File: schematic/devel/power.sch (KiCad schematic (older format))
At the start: 26 parts

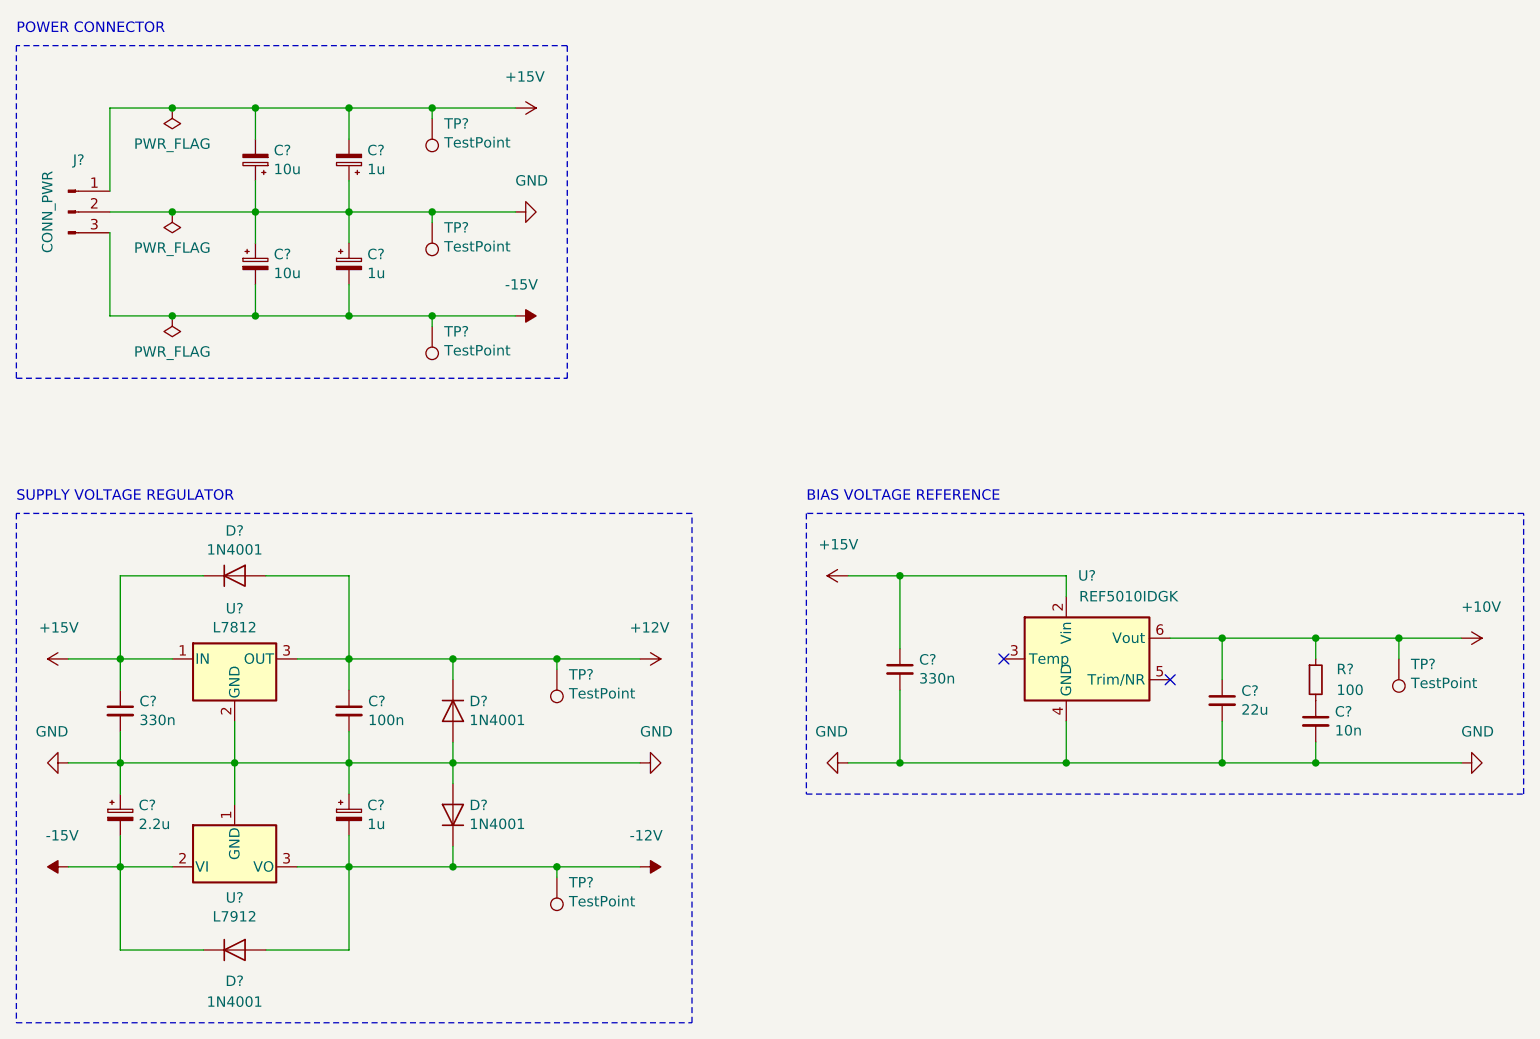
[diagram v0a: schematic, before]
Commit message: fixed floating buffer in arthimetic unit
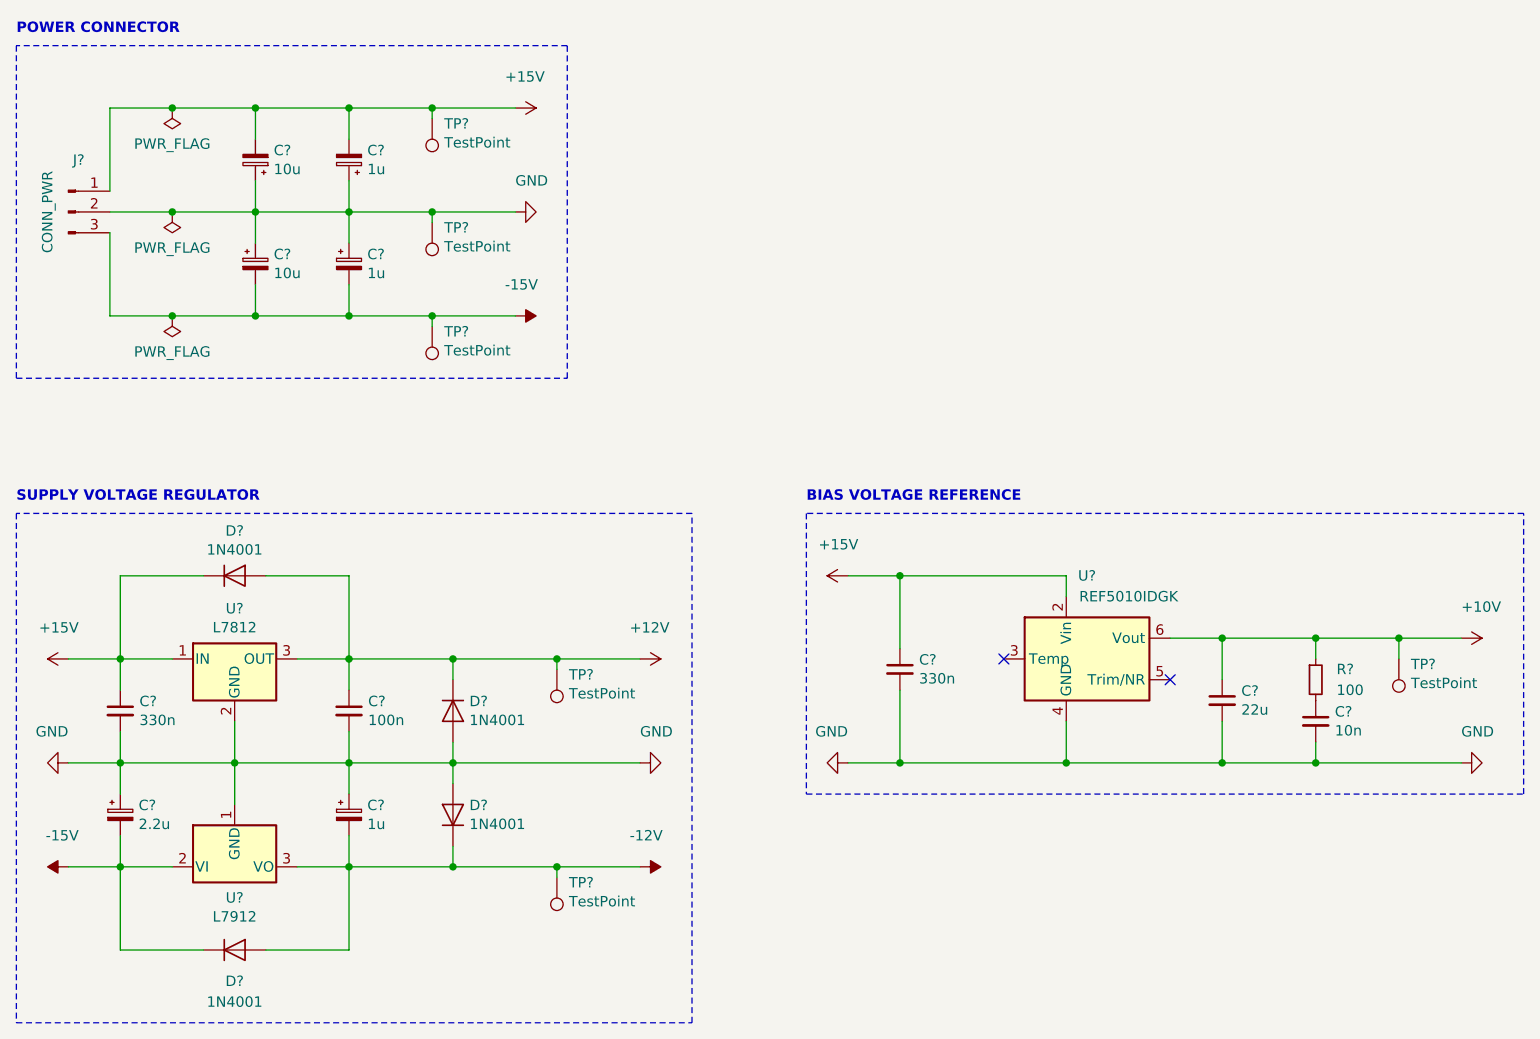
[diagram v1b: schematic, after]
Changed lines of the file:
@@
 Comment4 "Power Management"
 $EndDescr
-Text Notes 700  750  0    50   ~ 0
+Text Notes 700  750  0    50   ~ 6
 POWER CONNECTOR
 Wire Notes Line
@@
 P 3100 1600
 AR Path="/5D81CCB3" Ref="#PWR?"  Part="1"
-AR Path="/5D7CE105/5D81CCB3" Ref="#PWR?"  Part="1"
-F 0 "#PWR?" H 3100 1350 50  0001 C CNN
+AR Path="/5D7CE105/5D81CCB3" Ref="#PWR0101"  Part="1"
+F 0 "#PWR0101" H 3100 1350 50  0001 C CNN
 F 1 "GND" V 3250 1600 50  0000 R CNN
 F 2 "" H 3100 1600 50  0001 C CNN
@@
 P 3100 2100
 AR Path="/5D81CCD6" Ref="#PWR?"  Part="1"
-AR Path="/5D7CE105/5D81CCD6" Ref="#PWR?"  Part="1"
-F 0 "#PWR?" H 3100 2200 50  0001 C CNN
+AR Path="/5D7CE105/5D81CCD6" Ref="#PWR0102"  Part="1"
+F 0 "#PWR0102" H 3100 2200 50  0001 C CNN
 F 1 "-15V" V 2950 2050 50  0000 L CNN
 F 2 "" H 3100 2100 50  0001 C CNN
@@
 P 3100 1100
 AR Path="/5D81CCE3" Ref="#PWR?"  Part="1"
-AR Path="/5D7CE105/5D81CCE3" Ref="#PWR?"  Part="1"
-F 0 "#PWR?" H 3100 950 50  0001 C CNN
+AR Path="/5D7CE105/5D81CCE3" Ref="#PWR0103"  Part="1"
+F 0 "#PWR0103" H 3100 950 50  0001 C CNN
 F 1 "+15V" V 2950 1050 50  0000 L CNN
 F 2 "" H 3100 1100 50  0001 C CNN
@@
 P 1450 1100
 AR Path="/5D81CD0E" Ref="#FLG?"  Part="1"
-AR Path="/5D7CE105/5D81CD0E" Ref="#FLG?"  Part="1"
-F 0 "#FLG?" H 1450 1175 50  0001 C CNN
+AR Path="/5D7CE105/5D81CD0E" Ref="#FLG0101"  Part="1"
+F 0 "#FLG0101" H 1450 1175 50  0001 C CNN
 F 1 "PWR_FLAG" H 1450 1273 50  0000 C CNN
 F 2 "" H 1450 1100 50  0001 C CNN
@@
 P 1450 2100
 AR Path="/5D81CD17" Ref="#FLG?"  Part="1"
-AR Path="/5D7CE105/5D81CD17" Ref="#FLG?"  Part="1"
-F 0 "#FLG?" H 1450 2175 50  0001 C CNN
+AR Path="/5D7CE105/5D81CD17" Ref="#FLG0102"  Part="1"
+F 0 "#FLG0102" H 1450 2175 50  0001 C CNN
 F 1 "PWR_FLAG" H 1450 2273 50  0000 C CNN
 F 2 "" H 1450 2100 50  0001 C CNN
@@
 P 1450 1600
 AR Path="/5D81CD22" Ref="#FLG?"  Part="1"
-AR Path="/5D7CE105/5D81CD22" Ref="#FLG?"  Part="1"
-F 0 "#FLG?" H 1450 1675 50  0001 C CNN
+AR Path="/5D7CE105/5D81CD22" Ref="#FLG0103"  Part="1"
+F 0 "#FLG0103" H 1450 1675 50  0001 C CNN
 F 1 "PWR_FLAG" H 1450 1773 50  0000 C CNN
 F 2 "" H 1450 1600 50  0001 C CNN
@@
 	1    0    0    -1
 $EndComp
-Text Notes 4500 3000 0    50   ~ 0
+Text Notes 4500 3000 0    50   ~ 6
 BIAS VOLTAGE REFERENCE
 Wire Wire Line
@@
 P 7650 3650
 AR Path="/5D891805" Ref="#PWR?"  Part="1"
-AR Path="/5D7CE105/5D891805" Ref="#PWR?"  Part="1"
-F 0 "#PWR?" H 7650 3500 50  0001 C CNN
+AR Path="/5D7CE105/5D891805" Ref="#PWR0104"  Part="1"
+F 0 "#PWR0104" H 7650 3500 50  0001 C CNN
 F 1 "+10V" V 7500 3650 50  0000 L CNN
 F 2 "" H 7650 3650 50  0001 C CNN
@@
 P 7650 4250
 AR Path="/5D89180D" Ref="#PWR?"  Part="1"
-AR Path="/5D7CE105/5D89180D" Ref="#PWR?"  Part="1"
-F 0 "#PWR?" H 7650 4000 50  0001 C CNN
+AR Path="/5D7CE105/5D89180D" Ref="#PWR0105"  Part="1"
+F 0 "#PWR0105" H 7650 4000 50  0001 C CNN
 F 1 "GND" V 7500 4250 50  0000 R CNN
 F 2 "" H 7650 4250 50  0001 C CNN
@@
 P 950 4250
 AR Path="/5D891881" Ref="#PWR?"  Part="1"
-AR Path="/5D7CE105/5D891881" Ref="#PWR?"  Part="1"
-F 0 "#PWR?" H 950 4000 50  0001 C CNN
+AR Path="/5D7CE105/5D891881" Ref="#PWR0106"  Part="1"
+F 0 "#PWR0106" H 950 4000 50  0001 C CNN
 F 1 "GND" V 1100 4250 50  0000 R CNN
 F 2 "" H 950 4250 50  0001 C CNN
@@
 P 950 4750
 AR Path="/5D891887" Ref="#PWR?"  Part="1"
-AR Path="/5D7CE105/5D891887" Ref="#PWR?"  Part="1"
-F 0 "#PWR?" H 950 4850 50  0001 C CNN
+AR Path="/5D7CE105/5D891887" Ref="#PWR0107"  Part="1"
+F 0 "#PWR0107" H 950 4850 50  0001 C CNN
 F 1 "-15V" V 800 4700 50  0000 L CNN
 F 2 "" H 950 4750 50  0001 C CNN
@@
 P 950 3750
 AR Path="/5D89188D" Ref="#PWR?"  Part="1"
-AR Path="/5D7CE105/5D89188D" Ref="#PWR?"  Part="1"
-F 0 "#PWR?" H 950 3600 50  0001 C CNN
+AR Path="/5D7CE105/5D89188D" Ref="#PWR0108"  Part="1"
+F 0 "#PWR0108" H 950 3600 50  0001 C CNN
 F 1 "+15V" V 800 3700 50  0000 L CNN
 F 2 "" H 950 3750 50  0001 C CNN
@@
 P 4700 3350
 AR Path="/5D891893" Ref="#PWR?"  Part="1"
-AR Path="/5D7CE105/5D891893" Ref="#PWR?"  Part="1"
-F 0 "#PWR?" H 4700 3200 50  0001 C CNN
+AR Path="/5D7CE105/5D891893" Ref="#PWR0109"  Part="1"
+F 0 "#PWR0109" H 4700 3200 50  0001 C CNN
 F 1 "+15V" V 4550 3300 50  0000 L CNN
 F 2 "" H 4700 3350 50  0001 C CNN
@@
 P 4700 4250
 AR Path="/5D891899" Ref="#PWR?"  Part="1"
-AR Path="/5D7CE105/5D891899" Ref="#PWR?"  Part="1"
-F 0 "#PWR?" H 4700 4000 50  0001 C CNN
+AR Path="/5D7CE105/5D891899" Ref="#PWR0110"  Part="1"
+F 0 "#PWR0110" H 4700 4000 50  0001 C CNN
 F 1 "GND" V 4850 4250 50  0000 R CNN
 F 2 "" H 4700 4250 50  0001 C CNN
@@
 P 3700 3750
 AR Path="/5D8918AA" Ref="#PWR?"  Part="1"
-AR Path="/5D7CE105/5D8918AA" Ref="#PWR?"  Part="1"
-F 0 "#PWR?" H 3700 3600 50  0001 C CNN
+AR Path="/5D7CE105/5D8918AA" Ref="#PWR0111"  Part="1"
+F 0 "#PWR0111" H 3700 3600 50  0001 C CNN
 F 1 "+12V" V 3550 3700 50  0000 L CNN
 F 2 "" H 3700 3750 50  0001 C CNN
@@
 P 3700 4250
 AR Path="/5D8918B0" Ref="#PWR?"  Part="1"
-AR Path="/5D7CE105/5D8918B0" Ref="#PWR?"  Part="1"
-F 0 "#PWR?" H 3700 4000 50  0001 C CNN
+AR Path="/5D7CE105/5D8918B0" Ref="#PWR0112"  Part="1"
+F 0 "#PWR0112" H 3700 4000 50  0001 C CNN
 F 1 "GND" V 3550 4250 50  0000 R CNN
 F 2 "" H 3700 4250 50  0001 C CNN
@@
 P 3700 4750
 AR Path="/5D8918B6" Ref="#PWR?"  Part="1"
-AR Path="/5D7CE105/5D8918B6" Ref="#PWR?"  Part="1"
-F 0 "#PWR?" H 3700 4850 50  0001 C CNN
+AR Path="/5D7CE105/5D8918B6" Ref="#PWR0113"  Part="1"
+F 0 "#PWR0113" H 3700 4850 50  0001 C CNN
 F 1 "-12V" V 3550 4700 50  0000 L CNN
 F 2 "" H 3700 4750 50  0001 C CNN
@@
 Wire Notes Line
 	3950 3050 700  3050
-Text Notes 700  3000 0    50   ~ 0
+Text Notes 700  3000 0    50   ~ 6
 SUPPLY VOLTAGE REGULATOR
 $EndSCHEMATC

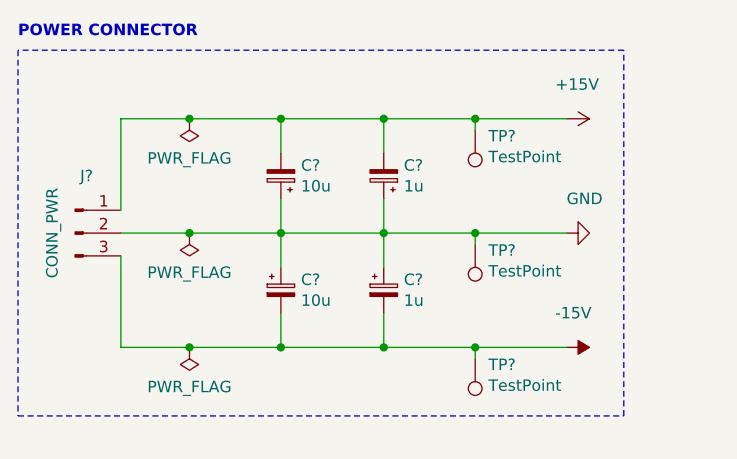
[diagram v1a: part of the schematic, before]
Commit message: fixed arithmetic typo, decoupling cap polarisation
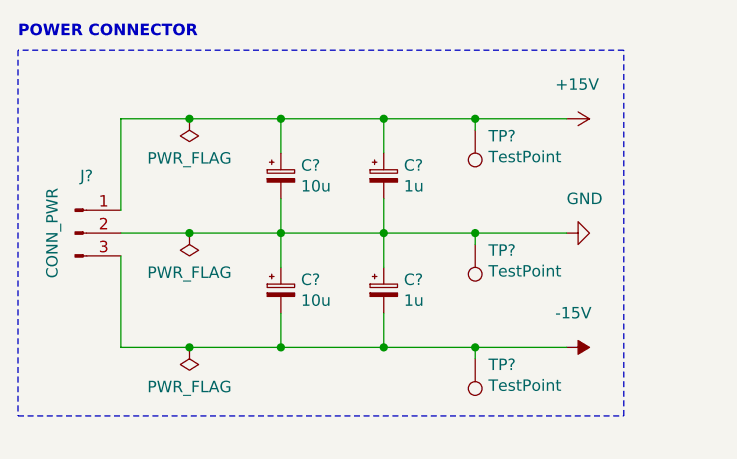
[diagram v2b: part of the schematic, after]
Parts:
- removed C?: 1u, symbol Device:CP_Small
- removed C?: 10u, symbol Device:CP_Small
- added C?: 10u, symbol Device:CP_Small
- added C?: 1u, symbol Device:CP_Small
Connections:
- net +15V: now also C?.1, C?.1
- net GND: now also C?.2, C?.2
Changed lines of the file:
@@
 Comment4 "Power Management"
 $EndDescr
-Text Notes 700  750  0    50   ~ 6
+Text Notes 700  750  0    50   ~ 10
 POWER CONNECTOR
 Wire Notes Line
@@
 Wire Wire Line
 	2300 1450 2300 1600
-$Comp
-L Device:CP_Small C?
-U 1 1 5D81CCBE
-P 2300 1350
-AR Path="/5D81CCBE" Ref="C?"  Part="1"
-AR Path="/5D7CE105/5D81CCBE" Ref="C?"  Part="1"
-F 0 "C?" H 2212 1304 50  0000 R CNN
-F 1 "1u" H 2212 1395 50  0000 R CNN
-F 2 "" H 2300 1350 50  0001 C CNN
-F 3 "~" H 2300 1350 50  0001 C CNN
-	1    2300 1350
-	-1   0    0    1
-$EndComp
 Wire Wire Line
 	1850 1450 1850 1600
-$Comp
-L Device:CP_Small C?
-U 1 1 5D81CCC5
-P 1850 1350
-AR Path="/5D81CCC5" Ref="C?"  Part="1"
-AR Path="/5D7CE105/5D81CCC5" Ref="C?"  Part="1"
-F 0 "C?" H 1762 1304 50  0000 R CNN
-F 1 "10u" H 1762 1395 50  0000 R CNN
-F 2 "" H 1850 1350 50  0001 C CNN
-F 3 "~" H 1850 1350 50  0001 C CNN
-	1    1850 1350
-	-1   0    0    1
-$EndComp
 Wire Wire Line
 	1850 1750 1850 1600
@@
 	1    0    0    -1
 $EndComp
-Text Notes 4500 3000 0    50   ~ 6
+Text Notes 4500 3000 0    50   ~ 10
 BIAS VOLTAGE REFERENCE
 Wire Wire Line
@@
 Wire Notes Line
 	3950 3050 700  3050
-Text Notes 700  3000 0    50   ~ 6
+Text Notes 700  3000 0    50   ~ 10
 SUPPLY VOLTAGE REGULATOR
+$Comp
+L Device:CP_Small C?
+U 1 1 5C9BC2C2
+P 1850 1350
+AR Path="/5C9BC2C2" Ref="C?"  Part="1"
+AR Path="/5D7CE105/5C9BC2C2" Ref="C?"  Part="1"
+F 0 "C?" H 1938 1396 50  0000 L CNN
+F 1 "10u" H 1938 1305 50  0000 L CNN
+F 2 "" H 1850 1350 50  0001 C CNN
+F 3 "~" H 1850 1350 50  0001 C CNN
+	1    1850 1350
+	1    0    0    -1
+$EndComp
+$Comp
+L Device:CP_Small C?
+U 1 1 5C9BC8E6
+P 2300 1350
+AR Path="/5C9BC8E6" Ref="C?"  Part="1"
+AR Path="/5D7CE105/5C9BC8E6" Ref="C?"  Part="1"
+F 0 "C?" H 2388 1396 50  0000 L CNN
+F 1 "1u" H 2388 1305 50  0000 L CNN
+F 2 "" H 2300 1350 50  0001 C CNN
+F 3 "~" H 2300 1350 50  0001 C CNN
+	1    2300 1350
+	1    0    0    -1
+$EndComp
 $EndSCHEMATC
